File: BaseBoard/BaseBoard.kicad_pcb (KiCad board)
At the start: 4 copper layers, 50 x 35 mm, 52 parts, among them J1 locked, J2 Serial Port, J3 add-on conn, Q1 PMN48XP, SW1 SW_DIP_x08, SW2 boot, SW3 Reset, U1 ESP32-WROOM-E, U2 4021, U3 MCP73831-2ACI-OT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

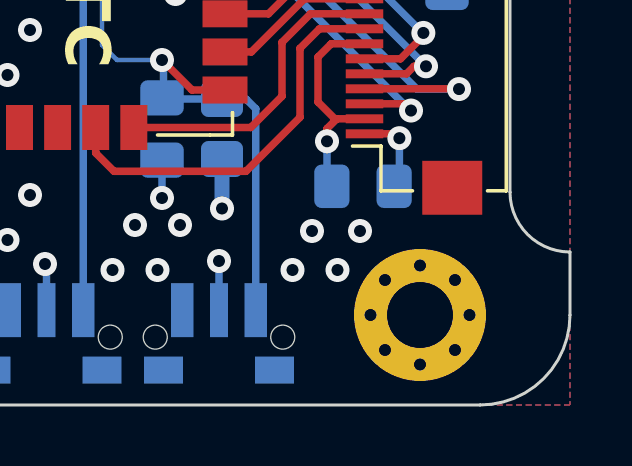
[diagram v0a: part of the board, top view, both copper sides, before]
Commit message: Moves bottom screw hole closer to the edge
Now that the gap is not as big we can move the screw hole closer to the
edge. This will not only make the board symmetrical, but also allow the
buttons to move closer to the edge to make more space for the battery in
the back.
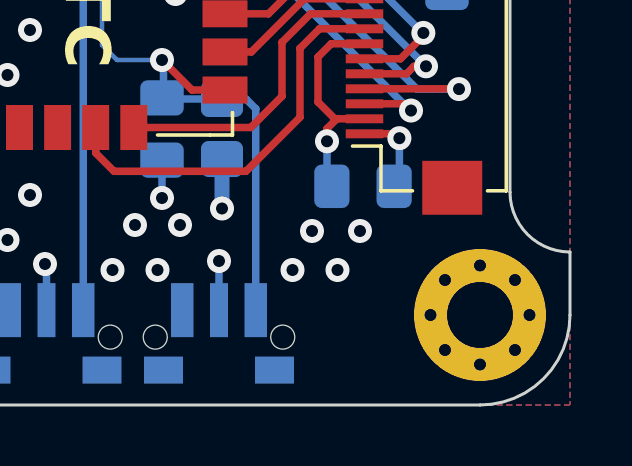
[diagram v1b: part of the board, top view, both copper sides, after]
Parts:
- moved H2 2.00 mm to (167.0, 112.0)
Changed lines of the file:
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@@
   )
   (footprint "MountingHole:MountingHole_2.2mm_M2_Pad_Via" locked (layer "F.Cu")
-    (at 165 112)
+    (at 167 112)
     (descr "Mounting Hole 2.2mm, M2")
     (tags "mounting hole 2.2mm m2")

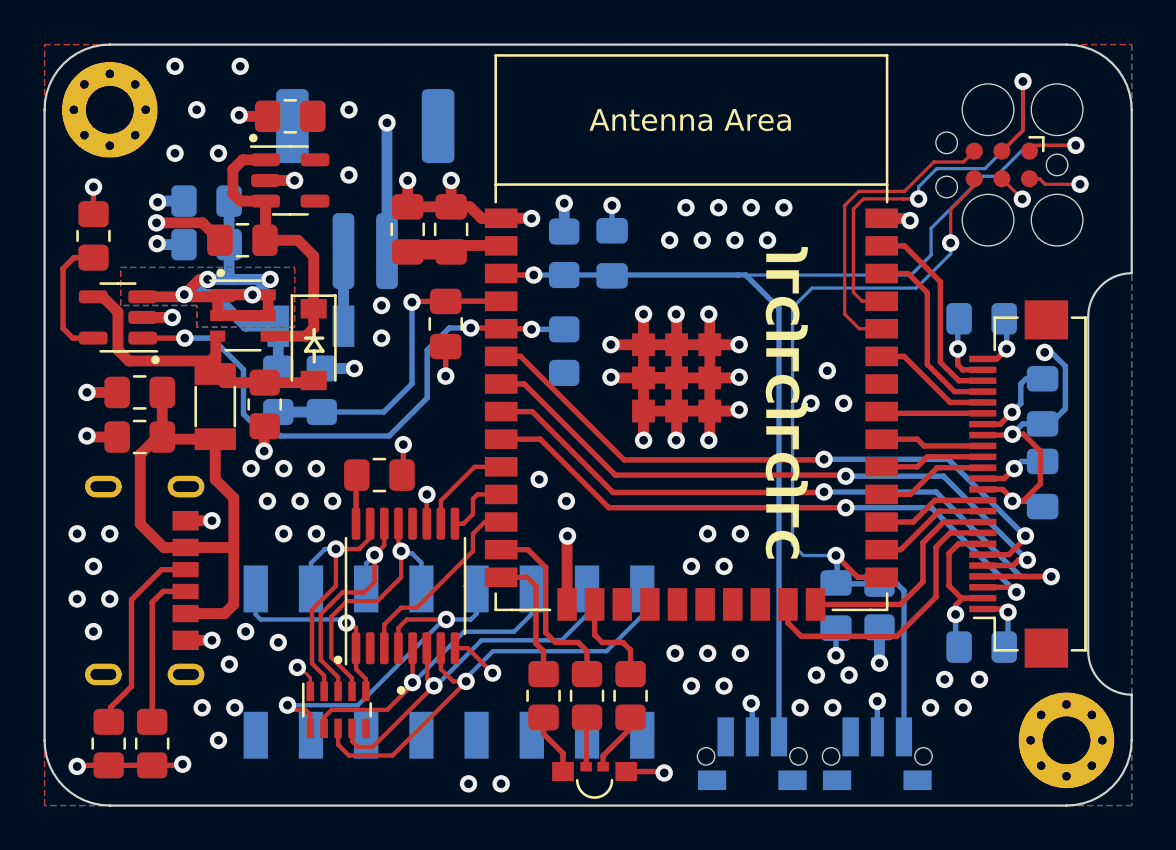
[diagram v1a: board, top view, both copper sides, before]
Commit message: Moves the tag-connect connector a bit more
This should improve the mechanical stability, as it's a little less
further into the PCB.
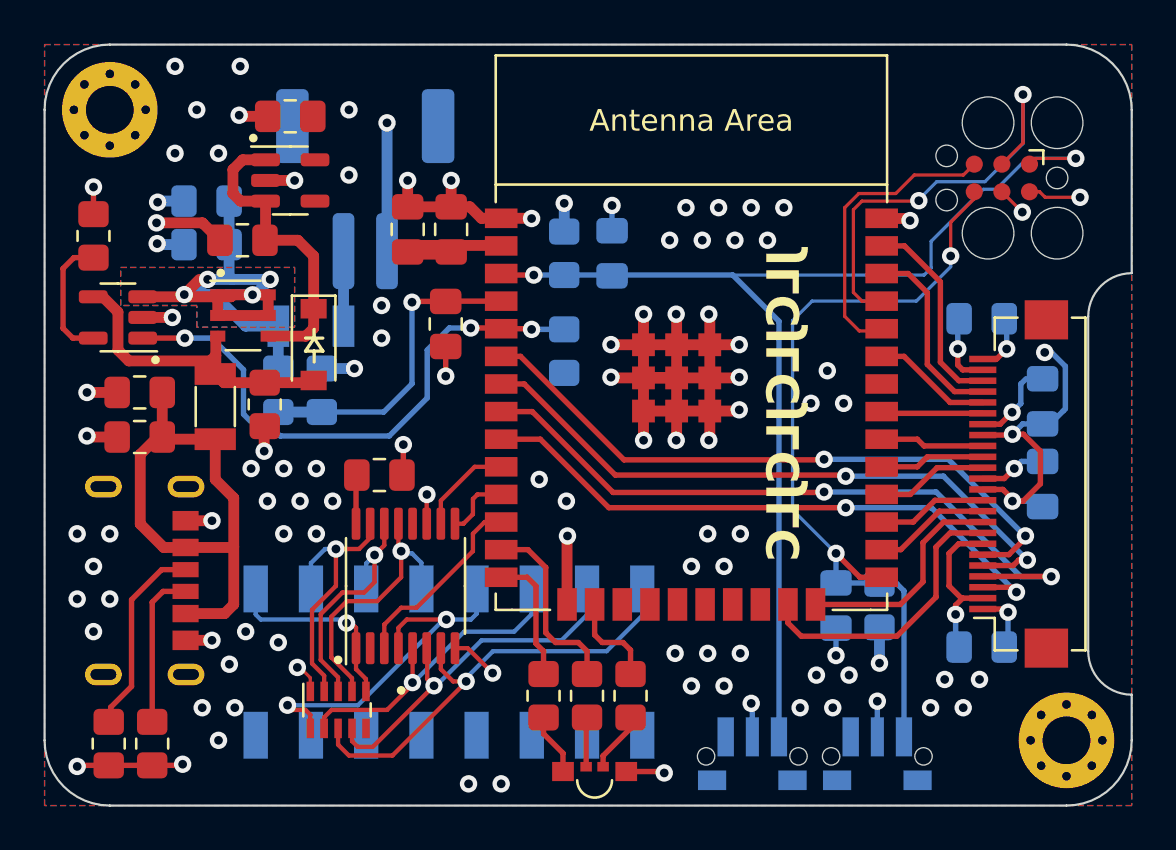
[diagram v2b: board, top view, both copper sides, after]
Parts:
- moved J2 0.60 mm to (164.0, 86.1)
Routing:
- net ESP_EN: track 54.1 -> 59.7 mm
- net ESP_BOOT: track 39.0 -> 37.6 mm
- net ESP_TX: track 20.8 -> 20.2 mm

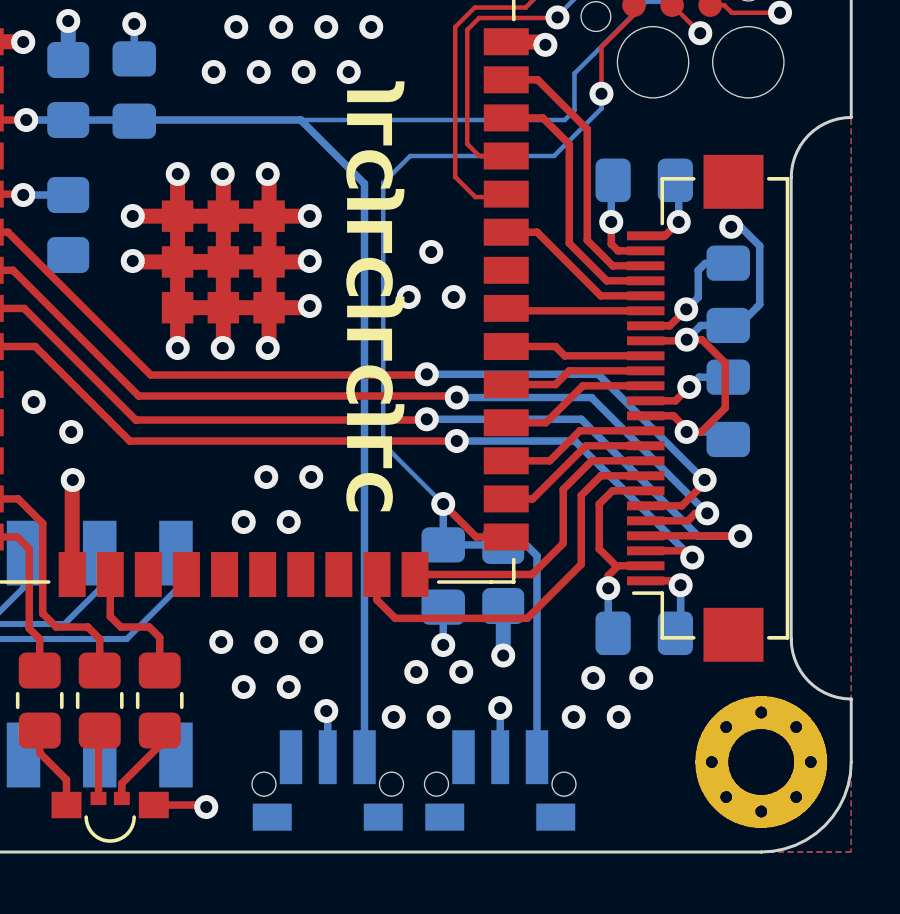
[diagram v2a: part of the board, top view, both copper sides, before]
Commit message: Moves boot and reset buttons further to the edge of the board
This will allow for more space in the center, where we could place the
battery when in an enclosure.
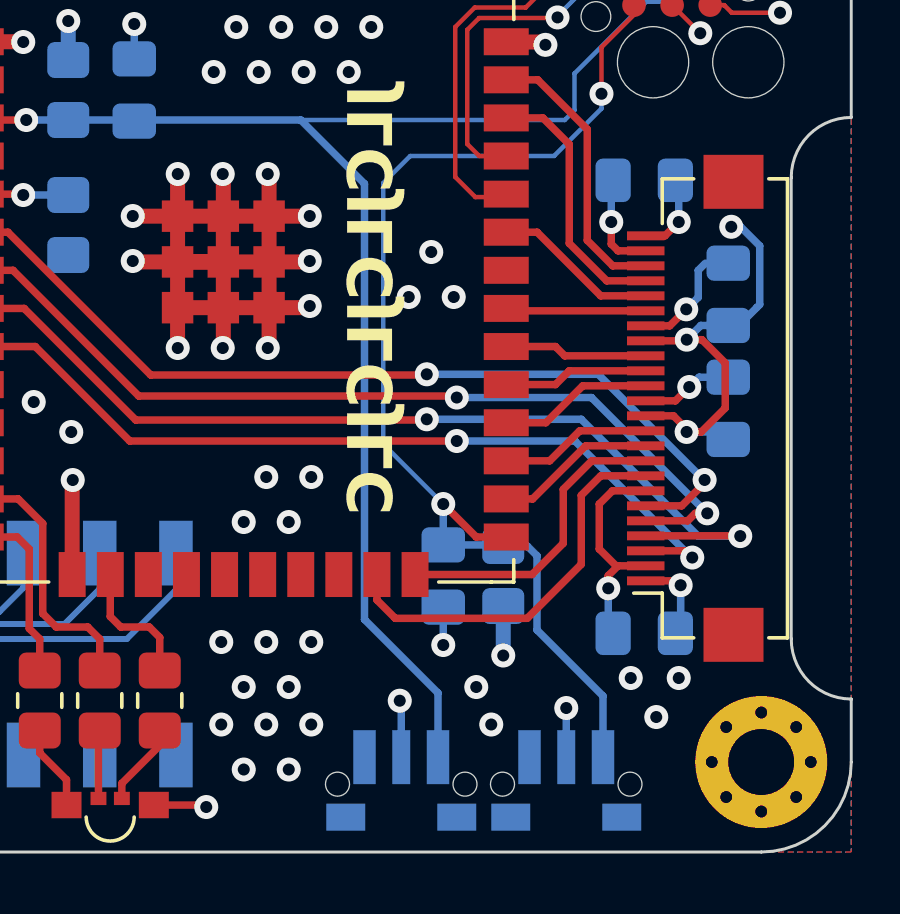
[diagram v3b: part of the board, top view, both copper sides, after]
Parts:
- moved kibuzzard-6253FE42 2.46 mm to (155.0, 109.8)
- moved SW3 2.45 mm to (155.0, 111.8)
- moved kibuzzard-6253FE4C 2.21 mm to (160.5, 109.8)
- moved SW2 2.20 mm to (160.5, 111.8)
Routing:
- net ESP_BOOT: track 37.6 -> 38.5 mm
- net +3V3: vias 70 -> 72

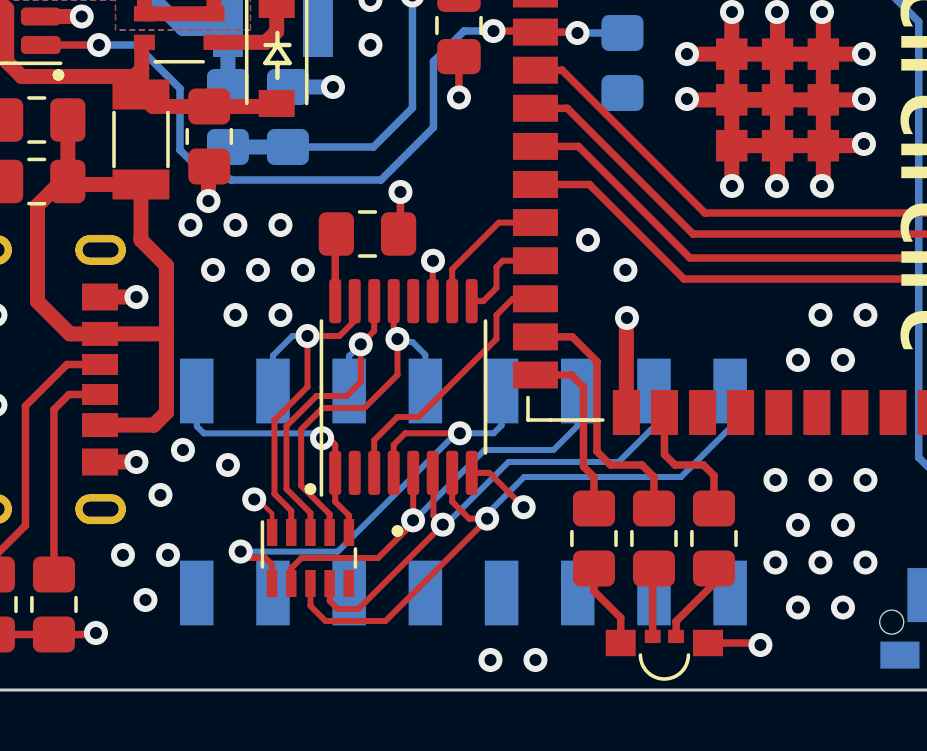
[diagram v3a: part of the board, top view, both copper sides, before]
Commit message: Removes vias and traces that were connected to ID circuit
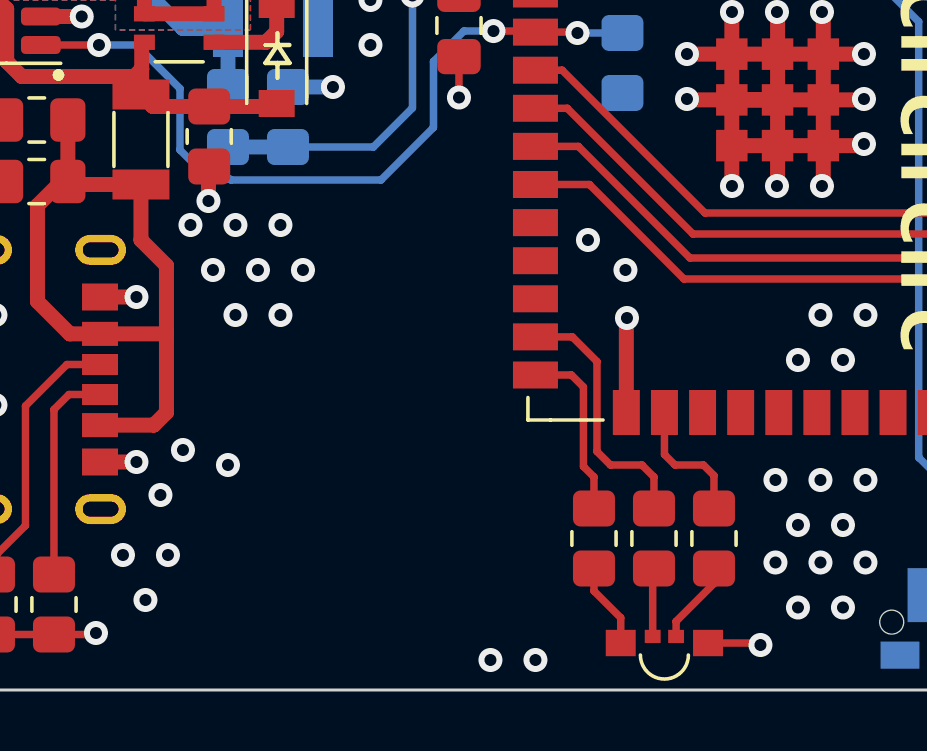
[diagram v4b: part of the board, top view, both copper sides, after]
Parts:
- removed C12: 100nF, Capacitor_SMD:C_0805_2012Metric_Pad1.18x1.45mm_HandSolder
- removed RN1: 10kΩ, GameOver:746X101
- removed Ref**: Val**, GameOver:logo_fsilk
- removed SW1: SW_DIP_x08, GameOver:DIP-16_CTS_219-8LPST
- removed U2: 4021, Package_SO:TSSOP-16_4.4x5mm_P0.65mm
- removed kibuzzard-6253FE1B: G***, kibuzzard-6253FE1B
- D2: value LED_RGBA -> LED_BGAR
- J3: value add-on conn -> base connector
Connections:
- D2 pad 1: Net-(D2-RK) -> Net-(D2-BK)
- D2 pad 3: Net-(D2-BK) -> +3V3
- D2 pad 4: +3V3 -> Net-(D2-RK)
- U1 pad 10: ID_CLK -> unconnected-(U1-DAC_1/ADC2_CH8/GPIO25)
- U1 pad 11: ID_LATCH -> unconnected-(U1-DAC_2/ADC2_CH9/GPIO26)
- U1 pad 12: ID_DATA -> unconnected-(U1-ADC2_CH7/GPIO27)
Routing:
- net Net-(RN1-R7): track 21.3 -> 0.00 mm, vias 1 -> 0
- net Net-(RN1-R8): track 17.1 -> 0.00 mm, vias 1 -> 0
- net Net-(RN1-R5): track 16.7 -> 0.00 mm, vias 2 -> 0
- net Net-(RN1-R6): track 14.8 -> 0.00 mm, vias 1 -> 0
- net Net-(RN1-R3): track 12.7 -> 0.00 mm, vias 1 -> 0
- net Net-(RN1-R1): track 12.3 -> 0.00 mm, vias 1 -> 0
- net Net-(RN1-R2): track 11.6 -> 0.00 mm, vias 1 -> 0
- net Net-(RN1-R4): track 9.16 -> 0.00 mm, vias 1 -> 0
- net ID_DATA: track 8.88 -> 0.00 mm
- net GND: track 109.1 -> 102.7 mm, vias 46 -> 42
- net ID_CLK: track 4.48 -> 0.00 mm
- net ID_LATCH: track 3.09 -> 0.00 mm
- net +3V3: track 37.5 -> 36.3 mm, vias 72 -> 71
- net Net-(D2-BK): track 2.85 -> 2.28 mm
- net Net-(D2-RK): track 2.28 -> 1.77 mm, vias 0 -> 1
